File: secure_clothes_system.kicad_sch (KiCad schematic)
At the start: 38 parts

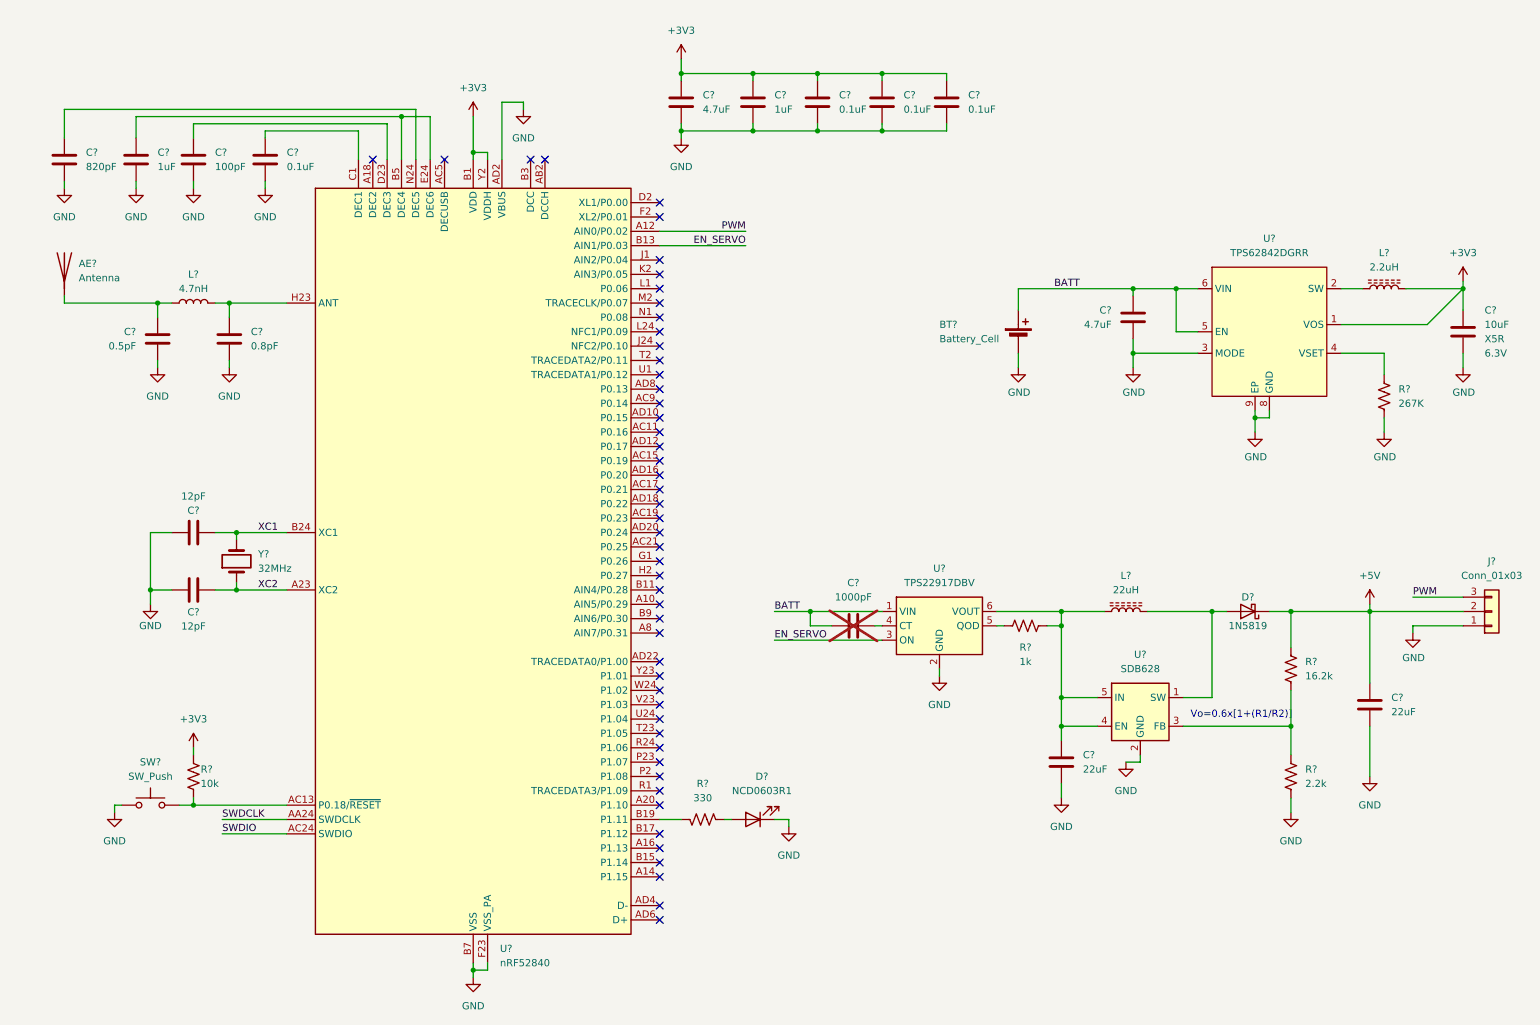
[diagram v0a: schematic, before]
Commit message: Made the components quote and found some alternatives for the MCU
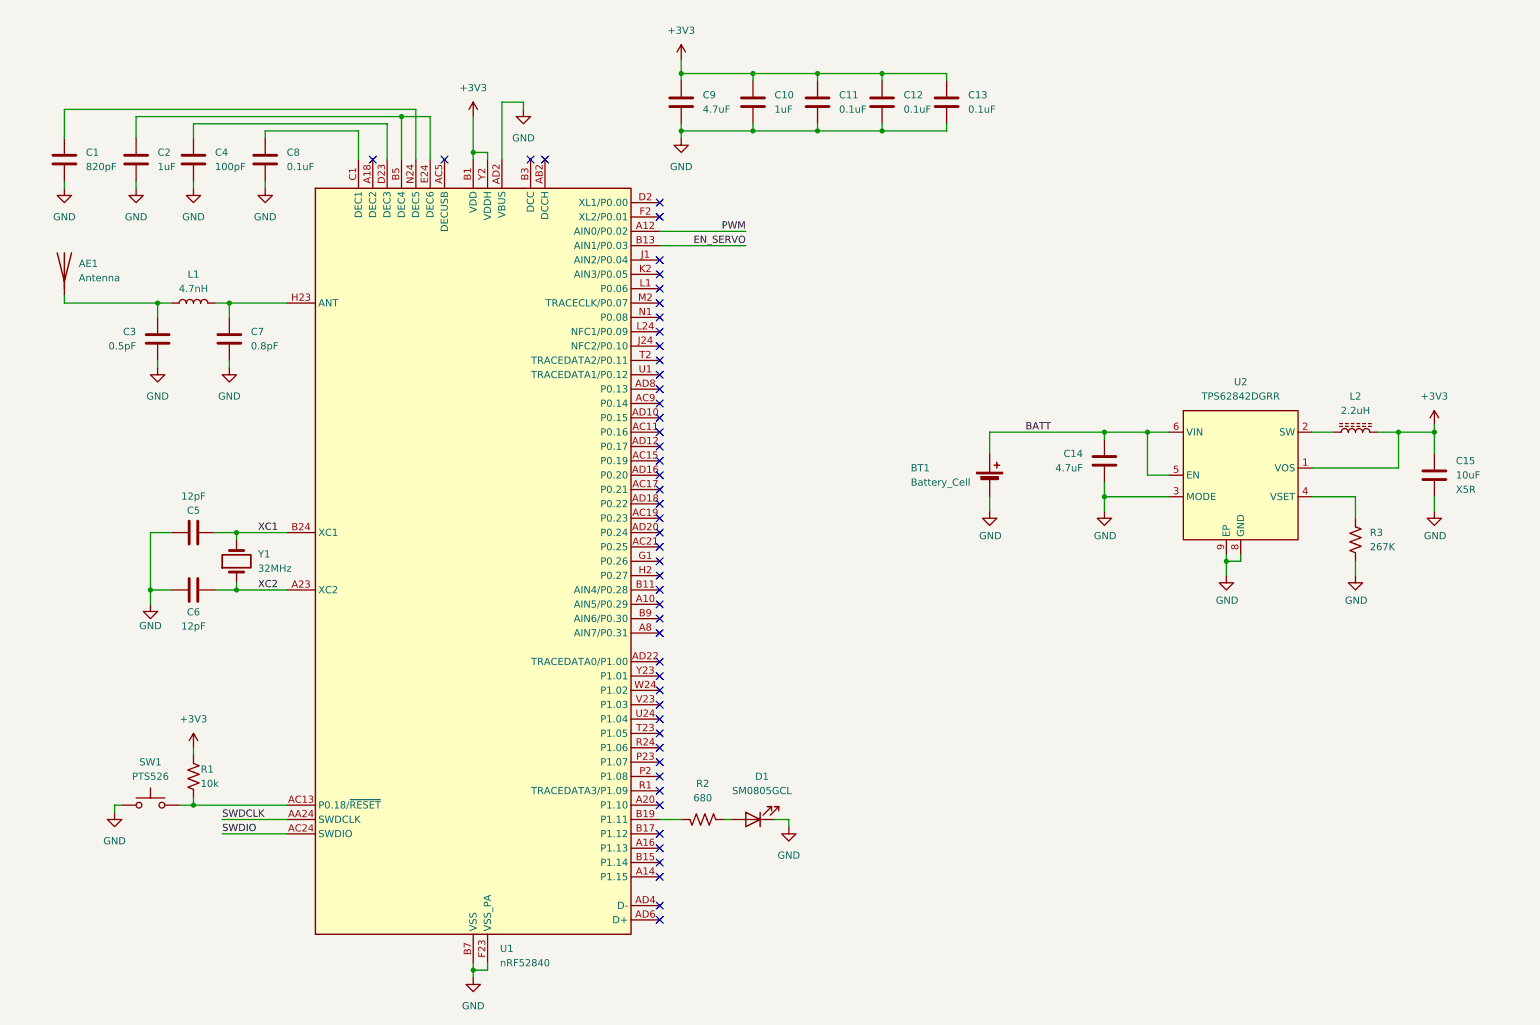
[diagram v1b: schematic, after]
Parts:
- removed C? (x2): 22uF, Capacitor_SMD:C_0805_2012Metric_Pad1.18x1.45mm_HandSolder, symbol Device:C
- removed C?: 1000pF, Capacitor_SMD:C_0603_1608Metric, symbol Device:C
- removed D?: 1N5819, Diode_SMD:D_SOD-123, symbol Diode:B120-E3
- removed J?: Conn_01x03, Connector_PinHeader_2.00mm:PinHeader_1x03_P2.00mm_Vertical, symbol Connector_Generic:Conn_01x03
- removed L?: 22uH, Inductor_SMD:L_Coilcraft_XxL4030, symbol Device:L_Ferrite
- removed R?: 1k, Resistor_SMD:R_0603_1608Metric, symbol componentes:Resistors/0603WAF1001T5E
- removed R?: 16.2k, Resistor_SMD:R_0603_1608Metric_Pad0.98x0.95mm_HandSolder, symbol Device:R_US
- removed R?: 2.2k, Resistor_SMD:R_0603_1608Metric_Pad0.98x0.95mm_HandSolder, symbol Device:R_US
- removed U?: TPS22917DBV, Package_TO_SOT_SMD:SOT-23-6, symbol Power_Management:TPS22917DBV
- removed U?: SDB628, Package_TO_SOT_SMD:SOT-23-6, symbol Regulator_Switching:MT3608
- C1: renamed from C?; footprint (none) -> Capacitor_SMD:C_0402_1005Metric; Descrip (none) -> CAP CER 820PF 50V C0G/NP0 0402; Manufacturer (none) -> Samsung Electro-Mechanics; Mfg Part # (none) -> CL05C821JB5NNNC; PROVIDER (none) -> Digikey; Price (none) -> 0.00841; TC (none) -> C0G, NP0; VOLTAGE (none) -> 50V
- C10, C2: renamed from C?; footprint (none) -> Capacitor_SMD:C_0603_1608Metric; Descrip (none) -> CAP CER 1UF 10V X7R 0603; Manufacturer (none) -> Samsung Electro-Mechanics; Mfg Part # (none) -> CL10B105KP8NNNC; PROVIDER (none) -> Digikey; Price (none) -> 0.00800; TC (none) -> X7R; VOLTAGE (none) -> 10V
- C11, C12, C13, C8: renamed from C?; footprint (none) -> Capacitor_SMD:C_0402_1005Metric; Descrip (none) -> CAP CER 0.1UF 10V X7R 0402; Manufacturer (none) -> Samsung Electro-Mechanics; Mfg Part # (none) -> CL05B104KP5NNNC; PROVIDER (none) -> Digikey; Price (none) -> 0.00400; TC (none) -> X7R; VOLTAGE (none) -> 10V
- C14: renamed from C?; footprint Capacitor_SMD:C_0603_1608Metric_Pad1.08x0.95mm_HandSolder -> Capacitor_SMD:C_0603_1608Metric; Descrip (none) -> CAP CER 4.7UF 10V X7R 0603; LCSC Part C1705 -> (none); Manufacturer Samsung Electro-Mechanics -> Murata Electronics; Mfg Part # (none) -> GRM188Z71A475ME15D; Mfr. Part CL10A475KP8NNNC -> (none); PROVIDER (none) -> Digikey; Price 0.01 -> 0.05912; TC (none) -> X7R; VOLTAGE (none) -> 10V
- C15: renamed from C?; footprint Capacitor_SMD:C_0805_2012Metric_Pad1.18x1.45mm_HandSolder -> Capacitor_SMD:C_0805_2012Metric; Descrip (none) -> CAP CER 10UF 10V X5R 0805; LCSC Part C17024 -> (none); Mfg Part # (none) -> CL21A106KPFNNNE; Mfr. Part CL21A106KPFNNNE -> (none); PROVIDER (none) -> Digikey; Price 0.01 -> 0.02060; V 6.3V -> (none); VOLTAGE (none) -> 10V
- C3: renamed from C?; footprint (none) -> Capacitor_SMD:C_0402_1005Metric; Descrip (none) -> CAP CER 8PF 50V C0G/NP0 0402; Manufacturer (none) -> Samsung Electro-Mechanics; Mfg Part # (none) -> CL05C080DB51PNC; PROVIDER (none) -> Digikey; Price (none) -> 0.01021; TC (none) -> C0G, NP0; VOLTAGE (none) -> 50V
- C4: renamed from C?; footprint (none) -> Capacitor_SMD:C_0402_1005Metric; Descrip (none) -> CAP CER 100PF 50V C0G/NPO 0402; Manufacturer (none) -> YAGEO; Mfg Part # (none) -> CC0402JRNPO9BN101; PROVIDER (none) -> Digikey; Price (none) -> 0.00400; TC (none) -> C0G, NP0; VOLTAGE (none) -> 50V
- C5, C6: renamed from C?; footprint (none) -> Capacitor_SMD:C_0402_1005Metric; Descrip (none) -> CAP CER 12PF 50V C0G/NP0 0402; Manufacturer (none) -> Murata Electronics; Mfg Part # (none) -> GRM1555C1H120GA01D; PROVIDER (none) -> Digikey; Price (none) -> 0.01063; TC (none) -> C0G, NP0; VOLTAGE (none) -> 50V
- C7: renamed from C?; footprint (none) -> Capacitor_SMD:C_0402_1005Metric; Descrip (none) -> CAP CER 0.8PF 50V C0G/NPO 0402; Manufacturer (none) -> YAGEO; Mfg Part # (none) -> CC0402BRNPO9BNR80; PROVIDER (none) -> Digikey; Price (none) -> 0.00613; TC (none) -> C0G, NP0; VOLTAGE (none) -> 50V
- C9: renamed from C?; footprint (none) -> Capacitor_SMD:C_0603_1608Metric; Descrip (none) -> CAP CER 4.7UF 10V X7R 0603; Manufacturer (none) -> Murata Electronics; Mfg Part # (none) -> GRM188Z71A475ME15D; PROVIDER (none) -> Digikey; Price (none) -> 0.05912; TC (none) -> X7R; VOLTAGE (none) -> 10V
- D1: renamed from D?; value NCD0603R1 -> SM0805GCL; footprint LED_SMD:LED_0603_1608Metric_Pad1.05x0.95mm_HandSolder -> Inductor_SMD:L_0805_2012Metric; CURRENT (none) -> 2mA; Descrip (none) -> LED GREEN CLEAR 0805 SMD; LCSC Part C84263 -> (none); Manufacturer Foshan NationStar Optoelectronics -> Bivar Inc.; Mfg Part # (none) -> SM0805GCL; Mfr. Part NCD0603R1 -> (none); PROVIDER (none) -> Digikey; Price 0.0082 -> 0.21700
- L1: renamed from L?; footprint (none) -> Inductor_SMD:L_0402_1005Metric; CURRENT (none) -> 750mA; Descrip (none) -> FIXED IND 4.7NH 750MA 70MOHM SMD; Manufacturer (none) -> Delta Electronics/Components; Mfg Part # (none) -> 0402HM-4N7EJTS; PROVIDER (none) -> Digikey; Price (none) -> 0.09197
- L2: renamed from L?; footprint Inductor_SMD:L_Taiyo-Yuden_MD-4040 -> Inductor_SMD:L_Murata_DFE201610P; CURRENT (none) -> 1.8A; Descrip (none) -> FIXED IND 2.2UH 1.8A 116MOHM SMD; LCSC Part C86081 -> (none); Mfg Part # (none) -> DFE201612E-2R2M=P2; Mfr. Part LQH44PN2R2MP0L -> (none); PROVIDER (none) -> Digikey; Price 0.14 -> 0.14588
- R1: renamed from R?; Descrip (none) -> RES 10K OHM 1% 1/10W 0603; LCSC Part C25804 -> (none); Manufacturer UNI-ROYAL(Uniroyal Elec) -> YAGEO; Mfg Part # (none) -> RC0603FR-0710KL; Mfr. Part 0603WAF1002T5E -> (none); PROVIDER (none) -> Digikey; Power (none) -> 0.1W, 1/10W; Price 0.0009 -> 0.00612
- R2: renamed from R?; value 330 -> 680; footprint Resistor_SMD:R_0603_1608Metric_Pad0.98x0.95mm_HandSolder -> Resistor_SMD:R_0603_1608Metric; Descrip (none) -> RES 680 OHM 5% 1/10W 0603; LCSC Part C23138 -> (none); Manufacturer UNI-ROYAL(Uniroyal Elec) -> YAGEO; Mfg Part # (none) -> RC0603JR-07680RL; Mfr. Part 0603WAF3300T5E -> (none); PROVIDER (none) -> Digikey; Power (none) -> 0.1W, 1/10W; Price 0.0011 -> 0.00408
- R3: renamed from R?; footprint Resistor_SMD:R_0603_1608Metric_Pad0.98x0.95mm_HandSolder -> Resistor_SMD:R_0603_1608Metric; Descrip (none) -> RES 267K OHM 1% 1/10W 0603; LCSC Part C2998118 -> (none); Manufacturer FOJAN -> YAGEO; Mfg Part # (none) -> RC0603FR-07267KL; Mfr. Part FRC0603F2673TS -> (none); PROVIDER (none) -> Digikey; Price 0.0010 -> 0.00510
- SW1: renamed from SW?; value SW_Push -> PTS526; footprint MR-footprint:SW_XUNPU_TS-1088R -> Button_Switch_SMD:SW_SPST_TL3342; Descrip (none) -> SWITCH TACTILE SPST-NO 0.05A 12V; LCSC Part C455280 -> (none); Manufacturer XUNPU -> C&K; Mfg Part # (none) -> PTS526SK15SMTR2 LFS; Mfr. Part TS-1088R-02026 -> (none); PROVIDER (none) -> Digikey; Price 0.0451 -> 0.09292
- U1: renamed from U?; Descrip (none) -> IC RF TXRX+MCU 802.15.4 73QFN; Manufacturer (none) -> Nordic Semiconductor ASA; Mfg Part # (none) -> NRF52840-QIAA-R; PROVIDER (none) -> Digikey; Price (none) -> 3.71002
- U2: renamed from U?; CURRENT (none) -> 750mA; Descrip (none) -> IC REG BUCK ADJ 750MA 8HVSSOP; LCSC Part C2873354 -> (none); Mfg Part # (none) -> TPS62842DGRR; Mfr. Part TPS62842DGRR -> (none); PROVIDER (none) -> Digikey; Price 1.73 -> 0.93834
- Y1: renamed from Y?; footprint (none) -> Crystal:Crystal_SMD_2016-4Pin_2.0x1.6mm; Descrip (none) -> 2.0MM X 1.6MM CRYSTAL 32MHZ 8PF; Manufacturer (none) -> KYOCERA AVX; Mfg Part # (none) -> CX2016SA32000D0KLRG1; PROVIDER (none) -> Digikey; Price (none) -> 0.23848
- gave numbers to parts that had none: 2
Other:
- note removed: "Vo=0.6x[1+(R1/R2)]"
- moved on the sheet: BT1, C14, C15, L2, R3, U2

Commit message: Made the components quote with the alternative ESP32-C3
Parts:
- removed AE1: Antenna, symbol Device:Antenna
- removed C1: 820pF, Capacitor_SMD:C_0402_1005Metric, symbol Device:C
- removed C10, C2: 1uF, Capacitor_SMD:C_0603_1608Metric, symbol Device:C
- removed C11, C12, C13, C8: 0.1uF, Capacitor_SMD:C_0402_1005Metric, symbol Device:C
- removed C3: 0.5pF, Capacitor_SMD:C_0402_1005Metric, symbol Device:C
- removed C4: 100pF, Capacitor_SMD:C_0402_1005Metric, symbol Device:C
- removed C5, C6: 12pF, Capacitor_SMD:C_0402_1005Metric, symbol Device:C
- removed C7: 0.8pF, Capacitor_SMD:C_0402_1005Metric, symbol Device:C
- removed C9: 4.7uF, Capacitor_SMD:C_0603_1608Metric, symbol Device:C
- removed D1: SM0805GCL, Inductor_SMD:L_0805_2012Metric, symbol componentes:Diode/NCD0603R1
- removed L1: 4.7nH, Inductor_SMD:L_0402_1005Metric, symbol Device:L
- removed R1: 10k, Resistor_SMD:R_0603_1608Metric, symbol componentes:Resistors/0603WAF1002T5E
- removed R2: 680, Resistor_SMD:R_0603_1608Metric, symbol componentes:Resistors/0603WAF3300T5E
- removed SW1: PTS526, Button_Switch_SMD:SW_SPST_TL3342, symbol Switch:SW_Push
- removed U1: nRF52840, Package_DFN_QFN:Nordic_AQFN-73-1EP_7x7mm_P0.5mm, symbol MCU_Nordic:nRF52840
- removed Y1: 32MHz, Crystal:Crystal_SMD_2016-4Pin_2.0x1.6mm, symbol Device:Crystal
- C1: renamed from C14; Mfg Part # GRM188Z71A475ME15D -> GRM188Z71A475KE15D; Price 0.05912 -> 0,05871; Tol (none) -> ±10%
- C2: renamed from C15; Price 0.02060 -> 0,02060
- L1: renamed from L2; Price 0.14588 -> 0,14588
- R1: renamed from R3; Price 0.00510 -> 0,00510
- U1: renamed from U2; Price 0.93834 -> 0,93834
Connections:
- no-connect marks 50 -> 0
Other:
- added sheet ESP32-C3 (modules/esp32-c3.kicad_sch)
- note added: "ESP32-C3"
- moved on the sheet: BT1, C1, C2, L1, R1, U1

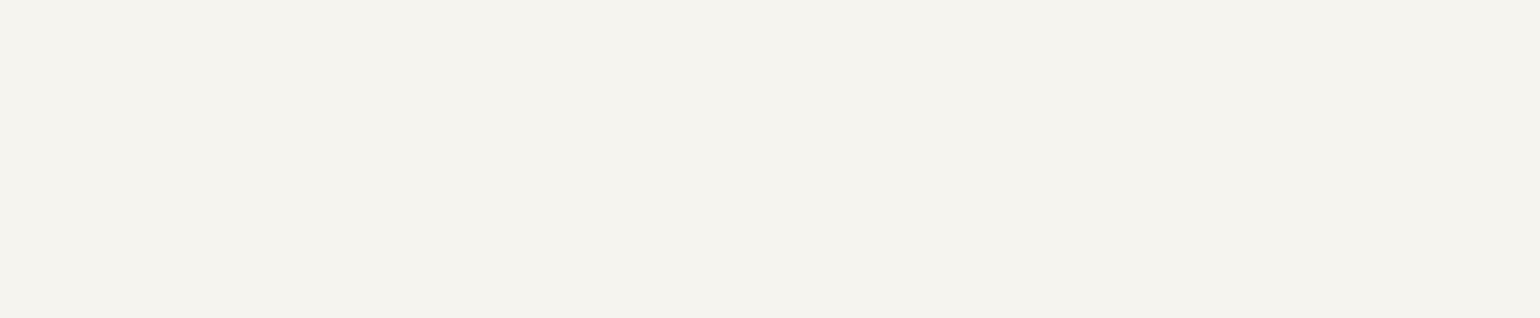
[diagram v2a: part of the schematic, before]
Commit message: Made the first version of the layout with the ESP32-C3
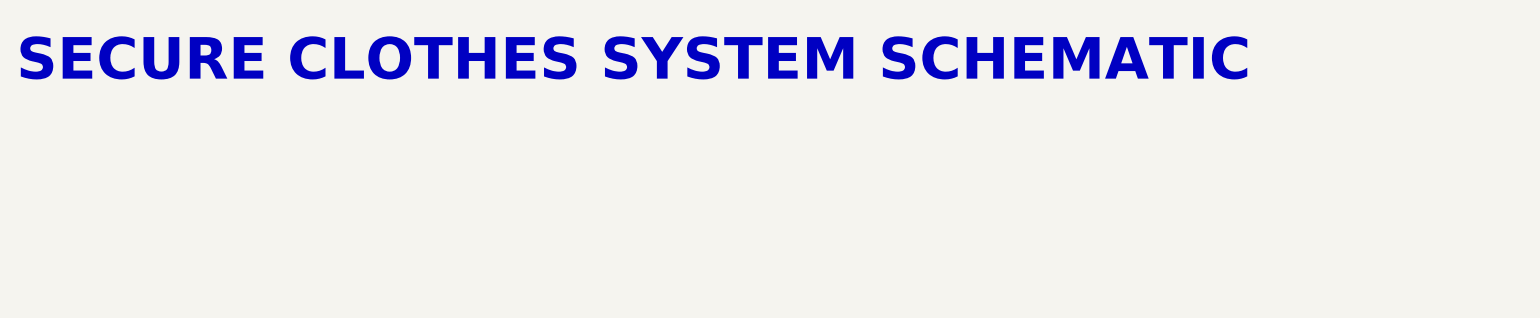
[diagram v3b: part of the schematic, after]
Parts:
- U1: symbol mr-powerSupply:TPS62842DGRR -> MSS_RegulatorLineal:TPS62842DGRR
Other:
- note added: "SECURE CLOTHES SYSTEM SCHEMATIC"
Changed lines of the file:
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@@
+		)
+	)
+	(text "SECURE CLOTHES SYSTEM SCHEMATIC"
+		(exclude_from_sim no)
+		(at 20.066 25.4 0)
+		(effects
+			(font
+				(size 5.08 5.08)
+				(thickness 1.016)
+				(bold yes)
+			)
+			(justify left bottom)
 		)
 	)
@@
 			)
 		)
-		(property "Description" ""
-			(at 138.43 90.17 0)
-			(effects
-				(font
-					(size 1.27 1.27)
-				)
-				(hide yes)
+		(property "Description" "Power symbol creates a global label with name \"+3V3\""
+			(at 138.43 90.17 0)
+			(effects
+				(font
+					(size 1.27 1.27)
+				)
+				(hide yes)
+			)
+		)
+		(property "Manufacturer" ""
+			(at 138.43 90.17 0)
+			(effects
+				(font
+					(size 1.27 1.27)
+				)
+				(hide yes)
+			)
+		)
+		(property "Mfg Part #" ""
+			(at 138.43 90.17 0)
+			(effects
+				(font
+					(size 1.27 1.27)
+				)
+				(hide yes)
+			)
+		)
+		(property "LCSC Part #" ""
+			(at 138.43 90.17 0)
+			(effects
+				(font
+					(size 1.27 1.27)
+				)
+				(hide yes)
+			)
+		)
+		(property "PROVIDER" ""
+			(at 138.43 90.17 0)
+			(effects
+				(font
+					(size 1.27 1.27)
+				)
+				(hide yes)
+			)
+		)
+		(property "Price" ""
+			(at 138.43 90.17 0)
+			(effects
+				(font
+					(size 1.27 1.27)
+				)
+				(hide yes)
+			)
+		)
+		(property "Descrip" ""
+			(at 138.43 90.17 0)
+			(effects
+				(font
+					(size 1.27 1.27)
+				)
+				(hide yes)
+			)
+		)
+		(property "PLACE" ""
+			(at 138.43 90.17 0)
+			(effects
+				(font
+					(size 1.27 1.27)
+				)
+			)
+		)
+		(property "VOLTAGE" ""
+			(at 138.43 90.17 0)
+			(effects
+				(font
+					(size 1.27 1.27)
+				)
+			)
+		)
+		(property "CURRENT" ""
+			(at 138.43 90.17 0)
+			(effects
+				(font
+					(size 1.27 1.27)
+				)
+			)
+		)
+		(property "TC" ""
+			(at 138.43 90.17 0)
+			(effects
+				(font
+					(size 1.27 1.27)
+				)
+			)
+		)
+		(property "Power" ""
+			(at 138.43 90.17 0)
+			(effects
+				(font
+					(size 1.27 1.27)
+				)
+			)
+		)
+		(property "Tol" ""
+			(at 138.43 90.17 0)
+			(effects
+				(font
+					(size 1.27 1.27)
+				)
 			)
 		)
@@
 	)
 	(symbol
-		(lib_id "mr-powerSupply:TPS62842DGRR")
+		(lib_id "MSS_RegulatorLineal:TPS62842DGRR")
 		(at 104.14 99.06 0)
 		(unit 1)
